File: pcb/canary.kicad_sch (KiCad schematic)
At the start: 22 parts, among them J1 Raspberry_Pi_4, J2 Conn_01x02_Pin, U1 TMP119AIYBGR, U2 BMP388, U3 SGP40-D-R4, U4 SHT4x, U5 CAT24C32WI-GT3

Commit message: complete pcb design (v1 fab), implement backend mqtt service
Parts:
- C1, C2, C3, C4, C5, C6, C7, C8: footprint Capacitor_SMD:C_0201_0603Metric -> Capacitor_SMD:C_0603_1608Metric
- D1: footprint LED_SMD:LED_0201_0603Metric -> LED_SMD:LED_0603_1608Metric
- R2, R3, R4, R5, R6: footprint Resistor_SMD:R_0201_0603Metric -> Capacitor_SMD:C_0603_1608Metric
- U4: footprint Sensor_Humidity:Sensirion_DFN-4_1.5x1.5mm_P0.8mm_SHT4x_NoCentralPad -> My_Footprints:DFN-4_L1.5-W1.5-P0.8-TL-EP
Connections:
- net +3.3V: now also U2.5 (SDO)
- net GND: no longer U2.5 (SDO)
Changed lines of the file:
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@@
 	(text "Pressure:"
 		(exclude_from_sim no)
-		(at 25.4 94.488 0)
+		(at 24.638 85.598 0)
 		(effects
 			(font
@@
 		(color 0 0 0 0)
 	)
+	(junction
+		(at 29.21 100.33)
+		(diameter 0)
+		(color 0 0 0 0)
+	)
 	(wire
 		(pts
@@
 	(wire
 		(pts
+			(xy 43.18 107.95) (xy 29.21 107.95)
+		)
+		(stroke
+			(width 0)
+			(type default)
+		)
+	)
+	(wire
+		(pts
 			(xy 215.9 45.72) (xy 215.9 39.37)
 		)
@@
 	(wire
 		(pts
+			(xy 29.21 107.95) (xy 29.21 100.33)
+		)
+		(stroke
+			(width 0)
+			(type default)
+		)
+	)
+	(wire
+		(pts
 			(xy 166.37 38.1) (xy 166.37 43.18)
 		)
@@
 	(wire
 		(pts
-			(xy 43.18 107.95) (xy 39.37 107.95)
-		)
-		(stroke
-			(width 0)
-			(type default)
-		)
-	)
-	(wire
-		(pts
-			(xy 39.37 107.95) (xy 39.37 113.03)
-		)
-		(stroke
-			(width 0)
-			(type default)
-		)
-	)
-	(wire
-		(pts
-			(xy 43.18 100.33) (xy 39.37 100.33)
+			(xy 43.18 100.33) (xy 29.21 100.33)
 		)
 		(stroke
@@
 	(wire
 		(pts
-			(xy 39.37 100.33) (xy 39.37 95.25)
+			(xy 29.21 100.33) (xy 29.21 93.98)
 		)
 		(stroke
@@
 			)
 		)
-		(property "Footprint" "Capacitor_SMD:C_0201_0603Metric"
+		(property "Footprint" "Capacitor_SMD:C_0603_1608Metric"
 			(at 120.65 138.43 0)
 			(effects
@@
 			)
 		)
-		(property "Footprint" "Capacitor_SMD:C_0201_0603Metric"
+		(property "Footprint" "Capacitor_SMD:C_0603_1608Metric"
 			(at 90.17 36.83 0)
 			(effects
@@
 			)
 		)
-		(property "Footprint" "Capacitor_SMD:C_0201_0603Metric"
+		(property "Footprint" "Capacitor_SMD:C_0603_1608Metric"
 			(at 67.31 139.7 0)
 			(effects
@@
 			)
 		)
-		(property "Footprint" "Resistor_SMD:R_0201_0603Metric"
+		(property "Footprint" "Capacitor_SMD:C_0603_1608Metric"
 			(at 264.16 104.14 0)
 			(effects
@@
 			)
 		)
-		(property "Footprint" "Resistor_SMD:R_0201_0603Metric"
+		(property "Footprint" "Capacitor_SMD:C_0603_1608Metric"
 			(at 173.99 60.96 0)
 			(effects
@@
 			)
 		)
-		(property "Footprint" "Sensor_Humidity:Sensirion_DFN-4_1.5x1.5mm_P0.8mm_SHT4x_NoCentralPad"
+		(property "Footprint" "My_Footprints:DFN-4_L1.5-W1.5-P0.8-TL-EP"
 			(at 114.3 154.94 0)
 			(effects
@@
 			)
 		)
-		(property "Footprint" "LED_SMD:LED_0201_0603Metric"
+		(property "Footprint" "LED_SMD:LED_0603_1608Metric"
 			(at 254 104.14 0)
 			(effects
@@
 			)
 		)
-		(property "Footprint" "Resistor_SMD:R_0201_0603Metric"
+		(property "Footprint" "Capacitor_SMD:C_0603_1608Metric"
 			(at 166.37 45.72 0)
 			(effects
@@
 			)
 		)
-		(property "Footprint" "Resistor_SMD:R_0201_0603Metric"
+		(property "Footprint" "Capacitor_SMD:C_0603_1608Metric"
 			(at 184.15 41.91 0)
 			(effects
@@
 			)
 		)
-		(property "Footprint" "Resistor_SMD:R_0201_0603Metric"
+		(property "Footprint" "Capacitor_SMD:C_0603_1608Metric"
 			(at 74.93 39.37 0)
 			(effects
@@
 	)
 	(symbol
-		(lib_id "power:GND")
-		(at 39.37 113.03 0)
-		(unit 1)
-		(exclude_from_sim no)
-		(in_bom yes)
-		(on_board yes)
-		(dnp no)
-		(fields_autoplaced yes)
-		(property "Reference" "#PWR010"
-			(at 39.37 119.38 0)
-			(effects
-				(font
-					(size 1.27 1.27)
-				)
-				(hide yes)
-			)
-		)
-		(property "Value" "GND"
-			(at 39.37 118.11 0)
-			(effects
-				(font
-					(size 1.27 1.27)
-				)
-			)
-		)
-		(property "Footprint" ""
-			(at 39.37 113.03 0)
-			(effects
-				(font
-					(size 1.27 1.27)
-				)
-				(hide yes)
-			)
-		)
-		(property "Datasheet" ""
-			(at 39.37 113.03 0)
-			(effects
-				(font
-					(size 1.27 1.27)
-				)
-				(hide yes)
-			)
-		)
-		(property "Description" "Power symbol creates a global label with name \"GND\" , ground"
-			(at 39.37 113.03 0)
-			(effects
-				(font
-					(size 1.27 1.27)
-				)
-				(hide yes)
-			)
-		)
-		(pin "1"
-		)
-		(instances
-			(project "canary"
-				(path "/a4817684-092e-4b1c-a55e-80cb81c55c67"
-					(reference "#PWR010")
-					(unit 1)
-				)
-			)
-		)
-	)
-	(symbol
 		(lib_id "Device:C_Small")
 		(at 82.55 95.25 90)
@@
 			)
 		)
-		(property "Footprint" "Capacitor_SMD:C_0201_0603Metric"
+		(property "Footprint" "Capacitor_SMD:C_0603_1608Metric"
 			(at 82.55 95.25 0)
 			(effects
@@
 			)
 		)
-		(property "Footprint" "Capacitor_SMD:C_0201_0603Metric"
+		(property "Footprint" "Capacitor_SMD:C_0603_1608Metric"
 			(at 222.25 45.72 0)
 			(effects
@@
 			)
 		)
-		(property "Footprint" "Capacitor_SMD:C_0201_0603Metric"
+		(property "Footprint" "Capacitor_SMD:C_0603_1608Metric"
 			(at 254 114.3 0)
 			(effects
@@
 			)
 		)
-		(property "Footprint" "Capacitor_SMD:C_0201_0603Metric"
+		(property "Footprint" "Capacitor_SMD:C_0603_1608Metric"
 			(at 82.55 90.17 0)
 			(effects
@@
 			)
 		)
-		(property "Footprint" "Capacitor_SMD:C_0201_0603Metric"
+		(property "Footprint" "Capacitor_SMD:C_0603_1608Metric"
 			(at 90.17 41.91 0)
 			(effects
@@
 	(symbol
 		(lib_id "power:+3.3V")
-		(at 39.37 95.25 0)
+		(at 29.21 93.98 0)
 		(unit 1)
 		(exclude_from_sim no)
@@
 		(fields_autoplaced yes)
 		(property "Reference" "#PWR011"
-			(at 39.37 99.06 0)
+			(at 29.21 97.79 0)
 			(effects
 				(font
@@
 		)
 		(property "Value" "+3.3V"
-			(at 39.37 90.17 0)
+			(at 29.21 88.9 0)
 			(effects
 				(font
@@
 		)
 		(property "Footprint" ""
-			(at 39.37 95.25 0)
+			(at 29.21 93.98 0)
 			(effects
 				(font
@@
 		)
 		(property "Datasheet" ""
-			(at 39.37 95.25 0)
+			(at 29.21 93.98 0)
 			(effects
 				(font
@@
 		)
 		(property "Description" "Power symbol creates a global label with name \"+3.3V\""
-			(at 39.37 95.25 0)
+			(at 29.21 93.98 0)
 			(effects
 				(font

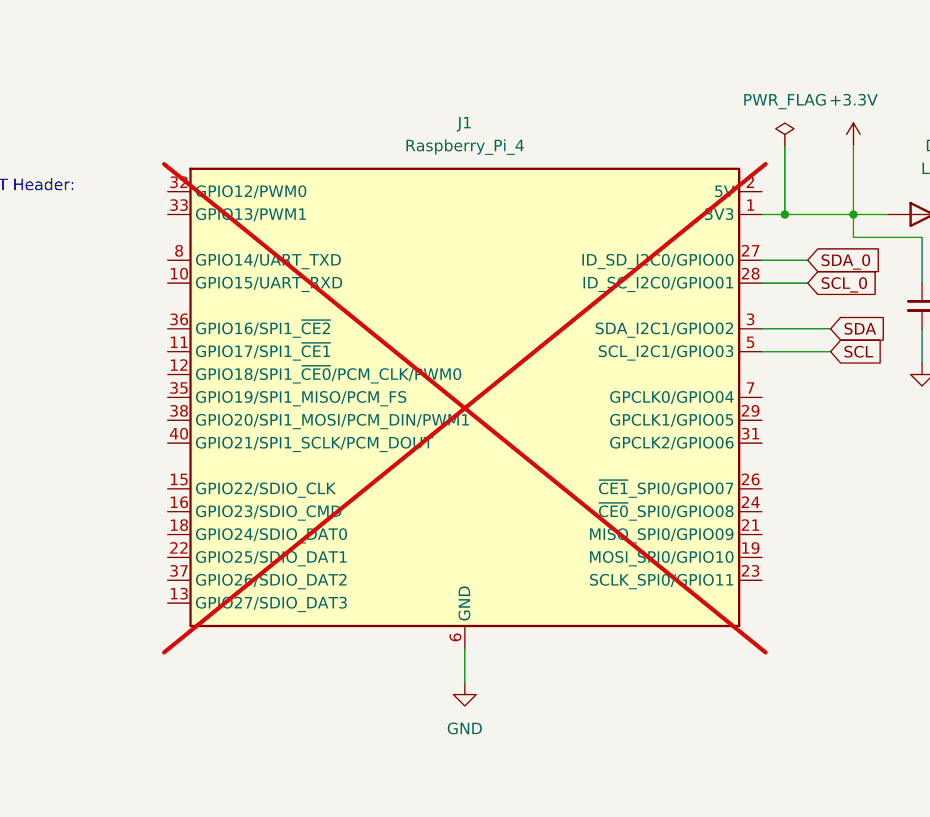
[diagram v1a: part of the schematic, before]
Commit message: update mqtt service to publish corrected temps, add temp data collection tool
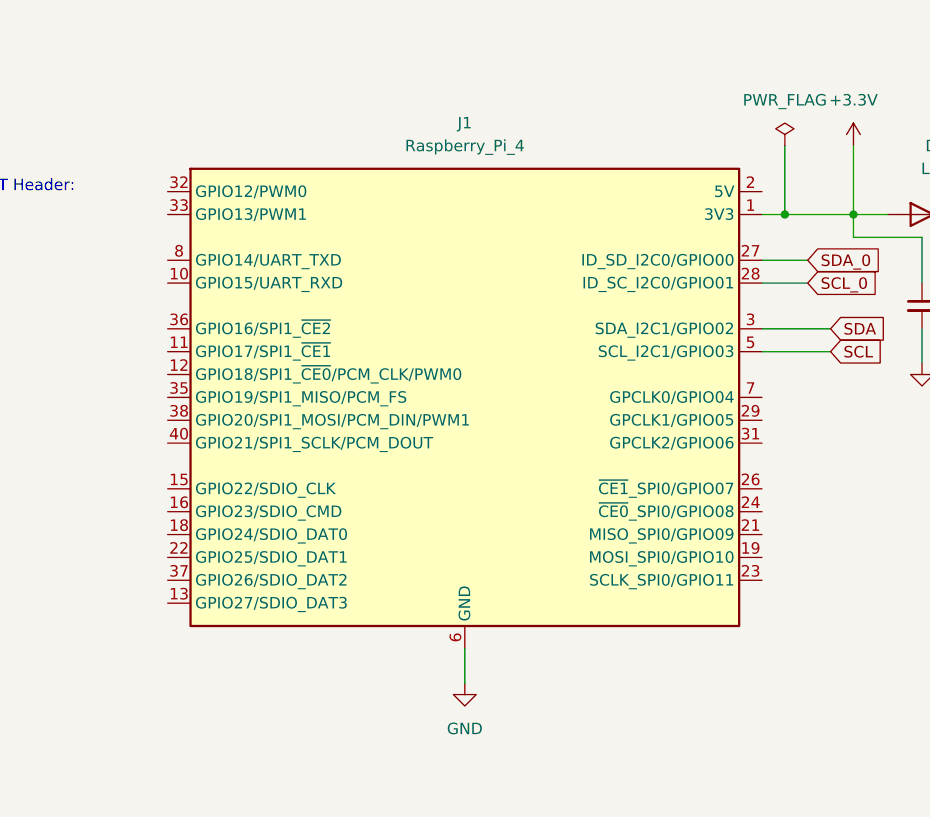
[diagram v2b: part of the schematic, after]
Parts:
- J1: now fitted
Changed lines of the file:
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@@
 		(in_bom yes)
 		(on_board yes)
-		(dnp yes)
+		(dnp no)
 		(fields_autoplaced yes)
 		(property "Reference" "J1"
